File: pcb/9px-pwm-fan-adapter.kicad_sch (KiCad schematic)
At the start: 7 parts

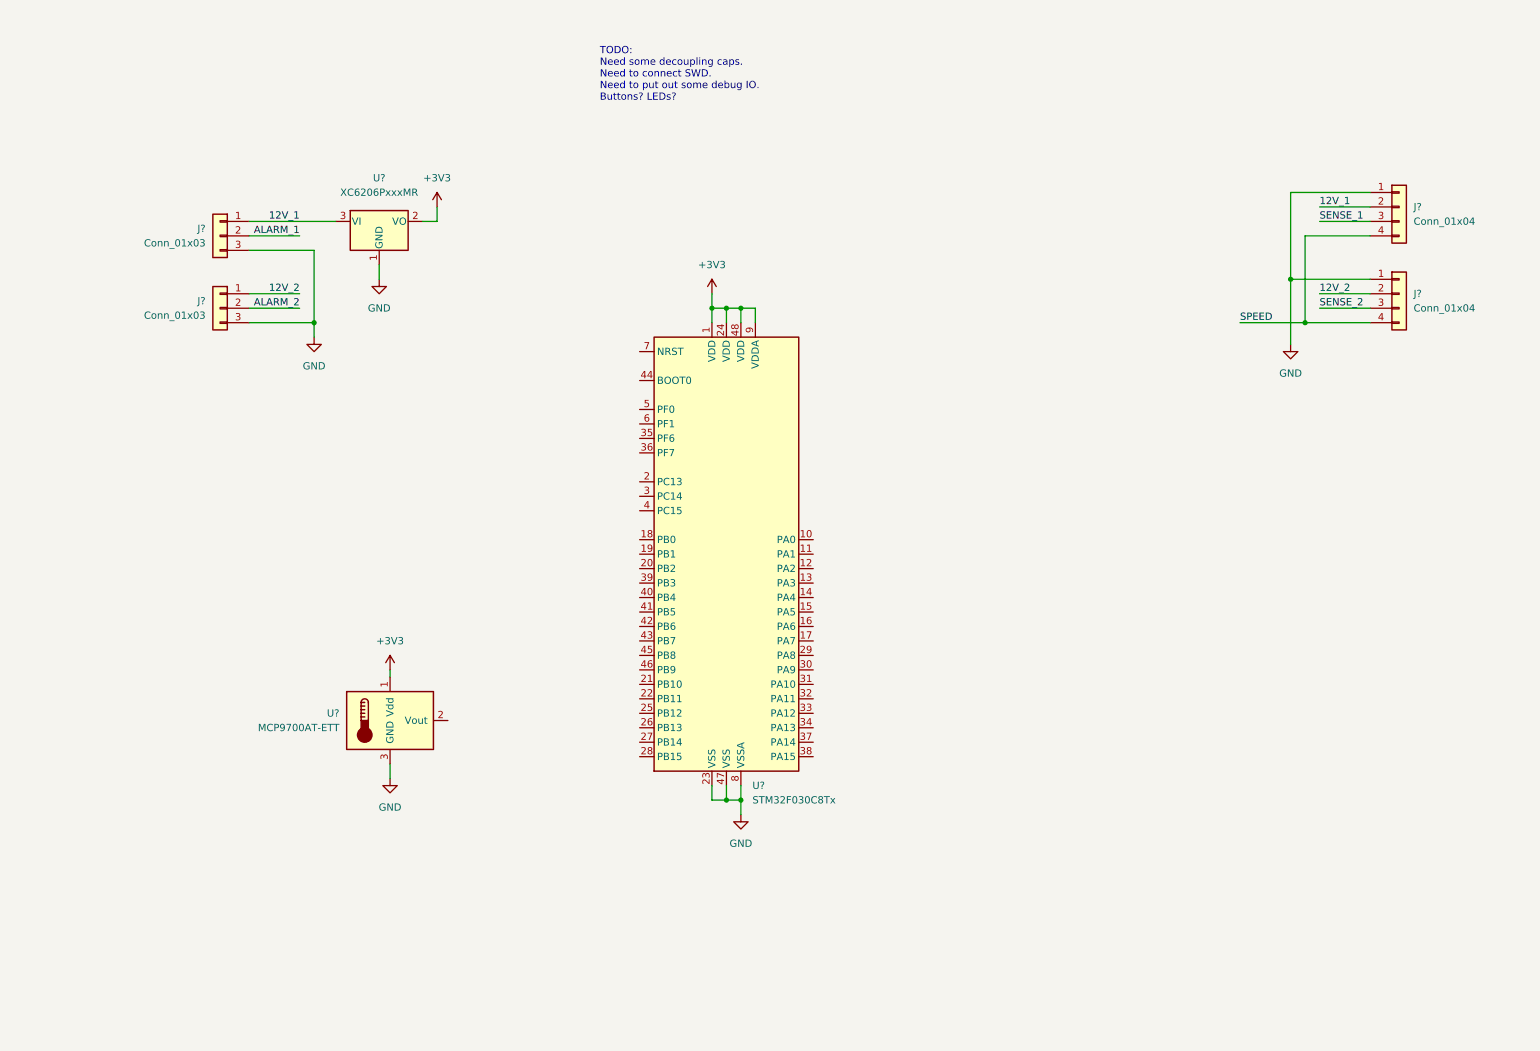
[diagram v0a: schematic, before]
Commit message: Schematic finished and moved to PCB design.
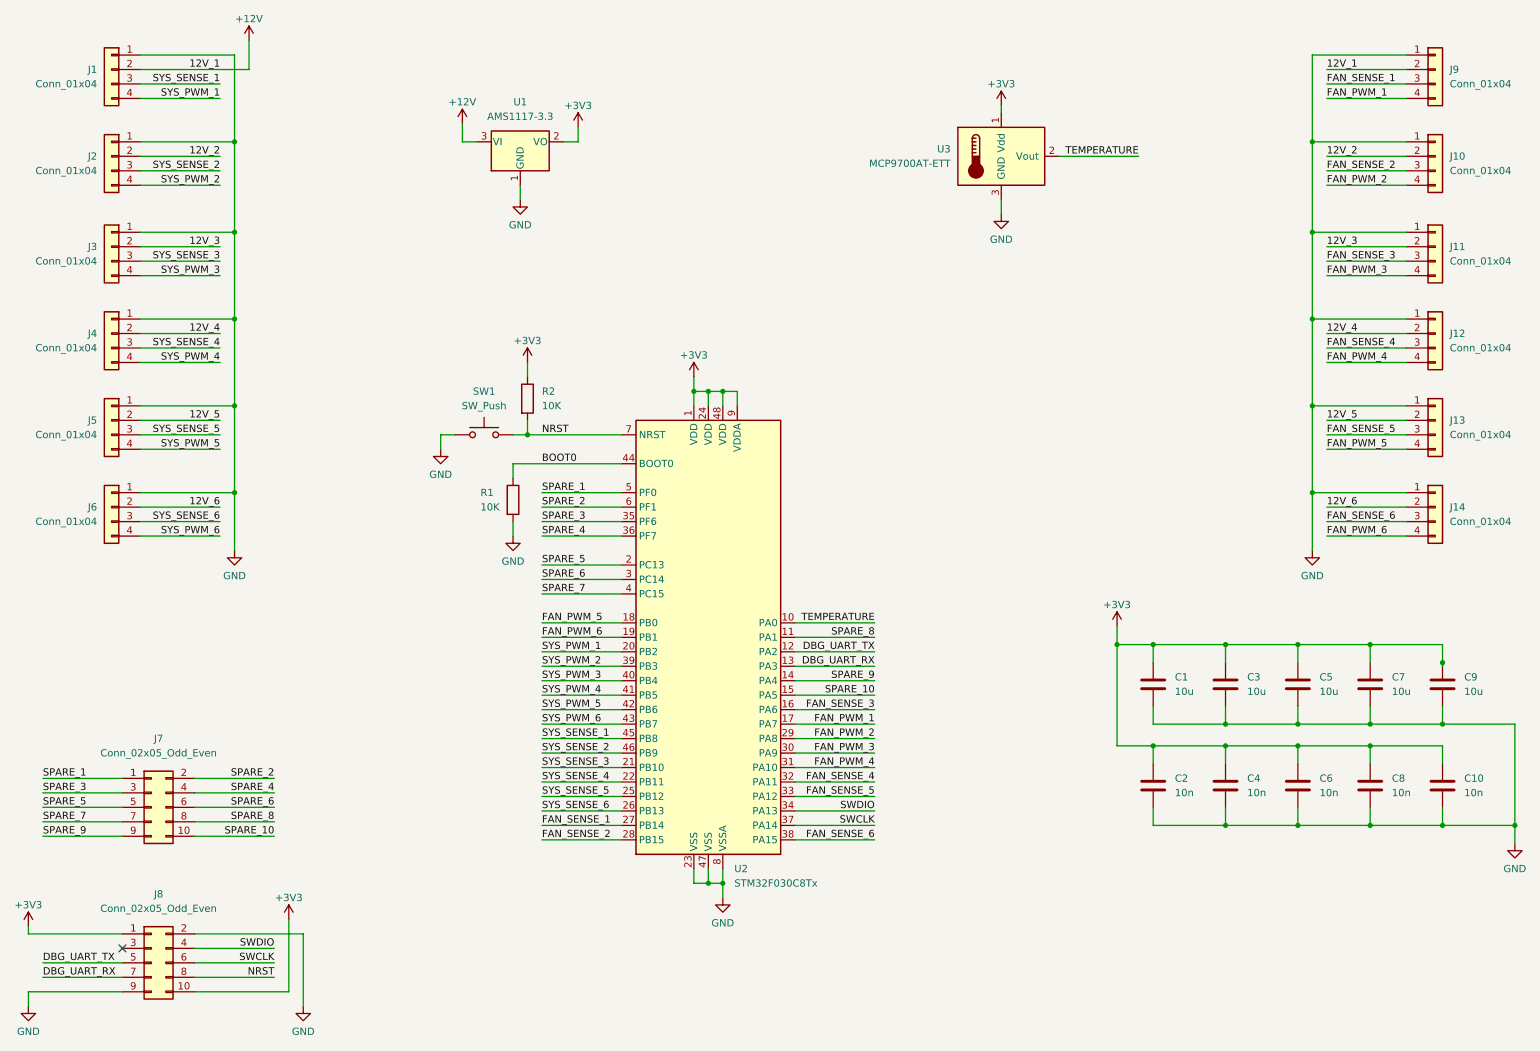
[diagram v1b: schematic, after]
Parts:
- removed J? (x2): Conn_01x03, symbol Connector_Generic:Conn_01x03
- removed U?: XC6206PxxxMR, Package_TO_SOT_SMD:SOT-23, symbol Regulator_Linear:XC6206PxxxMR
- added C1, C3, C5, C7, C9: 10u, Capacitor_SMD:C_0603_1608Metric, symbol Device:C
- added C10, C2, C4, C6, C8: 10n, Capacitor_SMD:C_0603_1608Metric, symbol Device:C
- added J1, J11, J12, J13, J14, J2, J3, J4, J5, J6: Conn_01x04, Connector_Molex:Molex_KK-254_AE-6410-04A_1x04_P2.54mm_Vertical, symbol Connector_Generic:Conn_01x04
- added J7, J8: Conn_02x05_Odd_Even, Connector_PinHeader_2.54mm:PinHeader_2x05_P2.54mm_Vertical, symbol Connector_Generic:Conn_02x05_Odd_Even
- added R1, R2: 10K, Resistor_SMD:R_0603_1608Metric, symbol Device:R
- added SW1: SW_Push, jlcpcb:SW-SMD_4P-L5.1-W5.1-P3.70-LS6.5-TL-2, symbol Switch:SW_Push
- added U1: AMS1117-3.3, Package_TO_SOT_SMD:SOT-223-3_TabPin2, symbol Regulator_Linear:AMS1117-3.3
- J10, J9: renamed from J?; footprint (none) -> Connector_Molex:Molex_KK-254_AE-6410-04A_1x04_P2.54mm_Vertical
- gave numbers to parts that had none: 2
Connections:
- net SENSE_1 is gone; now on net FAN_SENSE_1: J9.3 (Pin_3)
- net SENSE_2 is gone; now on net FAN_SENSE_2: J10.3 (Pin_3)
- net +3V3: now also C1.1, C10.1, C2.1, C3.1, C4.1, C5.1, C6.1, C7.1, C8.1, C9.1, J8.1 (Pin_1), J8.10 (Pin_10), R2.1, U1.2 (VO)
- net 12V_2: now also J2.2 (Pin_2)
- net GND: now also C1.2, C10.2, C2.2, C3.2, C4.2, C5.2, C6.2, C7.2, C8.2, C9.2, J1.1 (Pin_1), J11.1 (Pin_1), J12.1 (Pin_1), J13.1 (Pin_1), J14.1 (Pin_1), J2.1 (Pin_1), J3.1 (Pin_1), J4.1 (Pin_1), J5.1 (Pin_1), J6.1 (Pin_1), J8.2 (Pin_2), J8.9 (Pin_9), R1.2, SW1.1, U1.1 (GND)
- net TEMPERATURE: now reaches U2.10 (PA0)
- net TEMPERATURE: now also U3.2 (Vout)
- net SPARE_8: now reaches U2.11 (PA1)
- net SPARE_8: now also J7.8 (Pin_8)
- net DBG_UART_TX: now reaches U2.12 (PA2)
- net DBG_UART_TX: now also J8.5 (Pin_5)
- net DBG_UART_RX: now reaches U2.13 (PA3)
- net DBG_UART_RX: now also J8.7 (Pin_7)
- net SPARE_9: now reaches U2.14 (PA4)
- net SPARE_9: now also J7.9 (Pin_9)
- net SPARE_10: now reaches U2.15 (PA5)
- net SPARE_10: now also J7.10 (Pin_10)
- net FAN_SENSE_3: now reaches U2.16 (PA6)
- net FAN_SENSE_3: now also J11.3 (Pin_3)
- net FAN_PWM_1: now reaches U2.17 (PA7)
- net FAN_PWM_1: now also J9.4 (Pin_4)
- net FAN_PWM_5: now reaches U2.18 (PB0)
- net FAN_PWM_5: now also J13.4 (Pin_4)
- net FAN_PWM_6: now reaches U2.19 (PB1)
- net FAN_PWM_6: now also J14.4 (Pin_4)
- net SPARE_5: now reaches U2.2 (PC13)
- net SPARE_5: now also J7.5 (Pin_5)
- net SYS_PWM_1: now reaches U2.20 (PB2)
- net SYS_PWM_1: now also J1.4 (Pin_4)
- net SYS_SENSE_3: now reaches U2.21 (PB10)
- net SYS_SENSE_3: now also J3.3 (Pin_3)
- net SYS_SENSE_4: now reaches U2.22 (PB11)
- net SYS_SENSE_4: now also J4.3 (Pin_3)
- net SYS_SENSE_5: now reaches U2.25 (PB12)
- net SYS_SENSE_5: now also J5.3 (Pin_3)
- net SYS_SENSE_6: now reaches U2.26 (PB13)
- net SYS_SENSE_6: now also J6.3 (Pin_3)
- net FAN_SENSE_1: now reaches U2.27 (PB14)
- net FAN_SENSE_2: now reaches U2.28 (PB15)
- net FAN_PWM_2: now reaches U2.29 (PA8)
- net FAN_PWM_2: now also J10.4 (Pin_4)
- net SPARE_6: now reaches U2.3 (PC14)
- net SPARE_6: now also J7.6 (Pin_6)
- net FAN_PWM_3: now reaches U2.30 (PA9)
- net FAN_PWM_3: now also J11.4 (Pin_4)
- net FAN_PWM_4: now reaches U2.31 (PA10)
- net FAN_PWM_4: now also J12.4 (Pin_4)
- net FAN_SENSE_4: now reaches U2.32 (PA11)
- net FAN_SENSE_4: now also J12.3 (Pin_3)
- net FAN_SENSE_5: now reaches U2.33 (PA12)
- net FAN_SENSE_5: now also J13.3 (Pin_3)
- net SWDIO: now reaches U2.34 (PA13)
- net SWDIO: now also J8.4 (Pin_4)
- net SPARE_3: now reaches U2.35 (PF6)
- net SPARE_3: now also J7.3 (Pin_3)
- net SPARE_4: now reaches U2.36 (PF7)
- net SPARE_4: now also J7.4 (Pin_4)
- net SWCLK: now reaches U2.37 (PA14)
- net SWCLK: now also J8.6 (Pin_6)
- net FAN_SENSE_6: now reaches U2.38 (PA15)
- net FAN_SENSE_6: now also J14.3 (Pin_3)
- net SYS_PWM_2: now reaches U2.39 (PB3)
- net SYS_PWM_2: now also J2.4 (Pin_4)
- net SPARE_7: now reaches U2.4 (PC15)
- net SPARE_7: now also J7.7 (Pin_7)
- net SYS_PWM_3: now reaches U2.40 (PB4)
- net SYS_PWM_3: now also J3.4 (Pin_4)
- net SYS_PWM_4: now reaches U2.41 (PB5)
- net SYS_PWM_4: now also J4.4 (Pin_4)
- net SYS_PWM_5: now reaches U2.42 (PB6)
- net SYS_PWM_5: now also J5.4 (Pin_4)
- net SYS_PWM_6: now reaches U2.43 (PB7)
- net SYS_PWM_6: now also J6.4 (Pin_4)
- net BOOT0: now reaches U2.44 (BOOT0)
- net BOOT0: now also R1.1
- net SYS_SENSE_1: now reaches U2.45 (PB8)
- net SYS_SENSE_1: now also J1.3 (Pin_3)
- net SYS_SENSE_2: now reaches U2.46 (PB9)
- net SYS_SENSE_2: now also J2.3 (Pin_3)
- net SPARE_1: now reaches U2.5 (PF0)
- net SPARE_1: now also J7.1 (Pin_1)
- net SPARE_2: now reaches U2.6 (PF1)
- net SPARE_2: now also J7.2 (Pin_2)
- net NRST: now reaches U2.7 (NRST)
- net NRST: now also J8.8 (Pin_8), R2.2, SW1.2
- net 12V_1 renamed +12V
- net +12V: now also J1.2 (Pin_2), U1.3 (VI)
- removed net SPEED: J10.4 (Pin_4), J9.4 (Pin_4)
- new net 12V_3: J11.2 (Pin_2), J3.2 (Pin_2)
- new net 12V_4: J12.2 (Pin_2), J4.2 (Pin_2)
- new net 12V_5: J13.2 (Pin_2), J5.2 (Pin_2)
- new net 12V_6: J14.2 (Pin_2), J6.2 (Pin_2)
- no-connect marks 0 -> 1
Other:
- note removed: "TODO: Need some decoupling caps. Need to connect SWD. Need to put out some debug IO. Buttons? LEDs?"
- moved on the sheet: J10, J9, U2, U3
